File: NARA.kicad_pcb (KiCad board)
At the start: 4 copper layers, 93.9 x 42.4 mm, 144 parts, among them K1 BATT, K10 TOF_LD, K11 TOF_LS, K12 TOF_RF, K13 TOF_RD, K14 TOF_RS, K2 K_FPC_52435-2471, K3 PROG, K5 K_PicoSPOX-3, K6 K_0002, K7 K_PicoSPOX-3, K8 K_0002, K9 TOF_LF, Q1 Q_0004, Q2 Q_0007, Q3 Q_0007, Q4 Q_0007, Q5 Q_0007, Q6 Q_0007, Q7 Q_0007, Q8 Q_0004, Q9 Q_0004, SW1 SW_SKQG, SW2 SW_SKQG, U1 U_LT8610ABIMSE-3.3, U10 QRE1113GR, U11 QRE1113GR, U12 QRE1113GR, U2 U_AP2204K-5.0TRG1, U3 LTC2944, U4 L6234, U5 L6234, U6 LTC2955TS8-1, U7 STM32H743VITx, U8 ICM-20689, U9 QRE1113GR

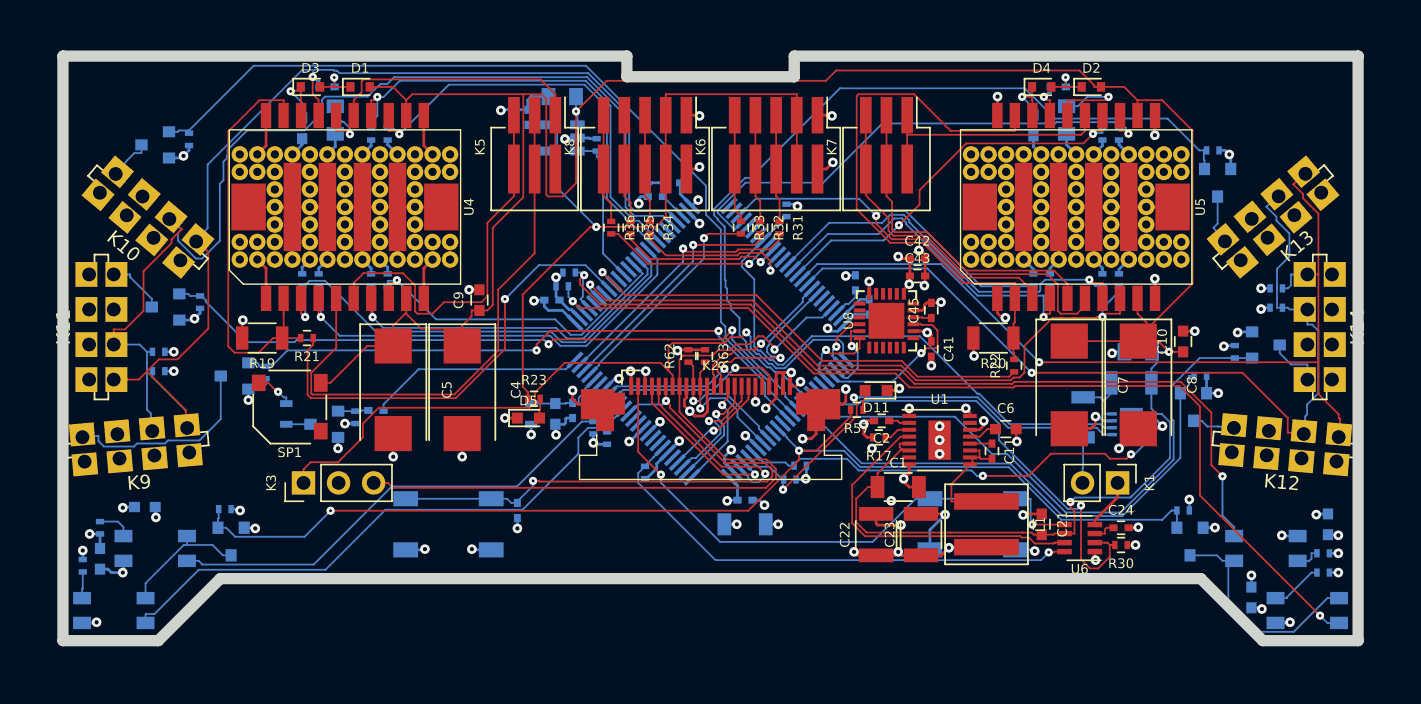
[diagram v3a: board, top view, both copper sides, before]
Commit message: Change EdgeCuts for TOF sensors, adapt power trace lengh
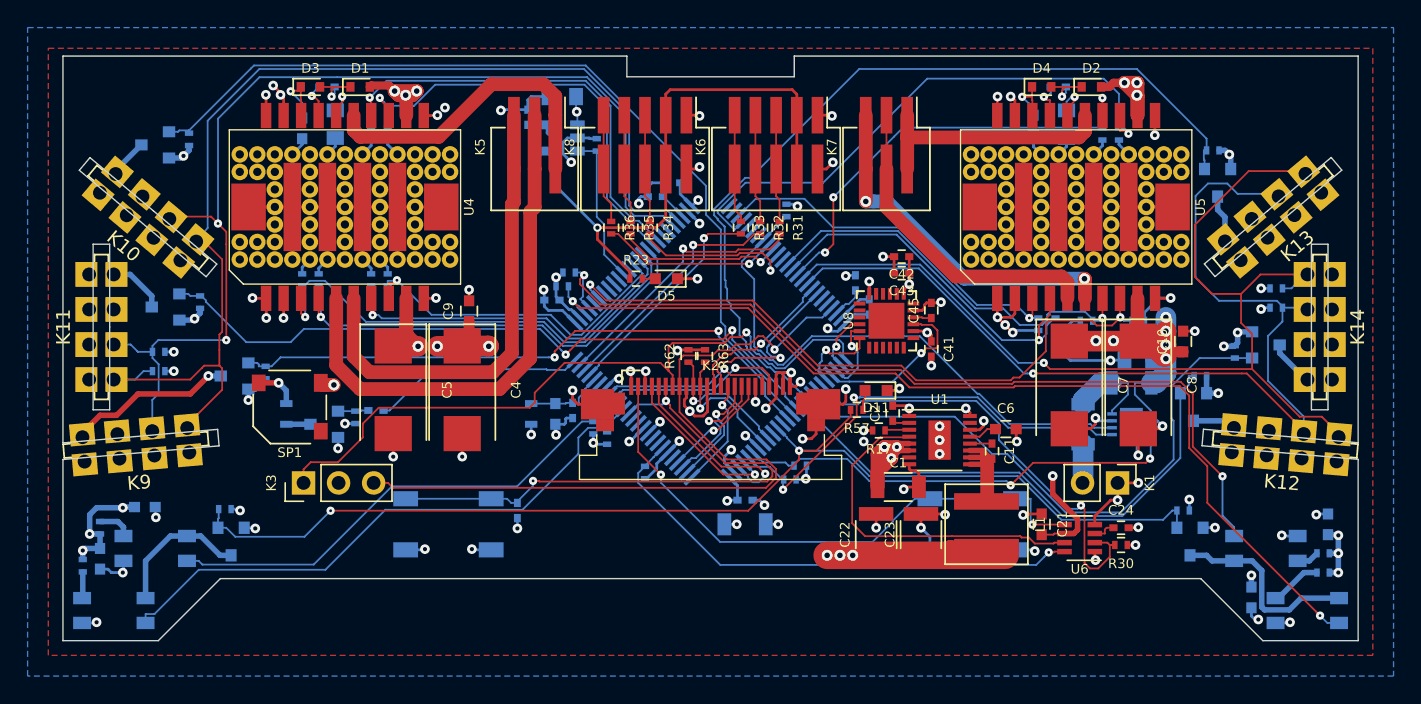
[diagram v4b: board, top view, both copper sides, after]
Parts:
- removed R19, R20: R_0093, DVB_Resistors:R_1206
- removed R21, R22: R_0015, DVB_Resistors:R_0402
- moved D5 14.2 mm to (94.8, 88.2), turned to 180 degrees
- moved R23 11.4 mm to (92.6, 88.2)
- moved R10 3.27 mm to (129.0, 91.2), turned to 180 degrees
- moved R4 3.22 mm to (123.0, 91.5), turned to 90 degrees
- moved R13 3.22 mm to (121.8, 91.5), turned to 90 degrees
- moved R2 3.17 mm to (125.2, 91.2), turned to 0 degrees
- moved C43 1.17 mm to (111.8, 87.8), turned to 180 degrees
- moved C42 1.16 mm to (111.8, 86.6), turned to 180 degrees
- moved C9 1.10 mm to (80.5, 90.5)
- moved C2 0.97 mm to (111.2, 98.0), turned to 90 degrees
- moved C17 0.60 mm to (129.0, 94.1)
- moved F1 0.50 mm to (125.0, 98.8)
- moved R17 0.50 mm to (110.2, 99.2)
- moved C15 0.30 mm to (70.8, 77.0)
- moved C16 0.30 mm to (123.8, 77.0)
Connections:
- U4 pad 19: Net-(R19-Pad1) -> GND
- U4 pad 2: Net-(R19-Pad1) -> GND
- U5 pad 19: Net-(R20-Pad1) -> GND
- U5 pad 2: Net-(R20-Pad1) -> GND
- U7 pad 33: /MOT_L_SENSE -> (no net)
- U7 pad 34: /MOT_R_SENSE -> (no net)
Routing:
- net Net-(R20-Pad1): track 41.2 -> 0.00 mm
- net GND: track 767.1 -> 801.5 mm, vias 76 -> 87
- net /MOT_R_SENSE: track 34.3 -> 0.00 mm, vias 1 -> 0
- net /MOT_L_SENSE: track 33.1 -> 0.00 mm, vias 1 -> 0
- net +BATT: track 189.7 -> 222.7 mm, vias 3 -> 22
- net Net-(R19-Pad1): track 30.4 -> 0.00 mm
- net +3.3V: track 323.2 -> 341.5 mm, vias 42 -> 41
- net /MOT_R_EN2: track 39.2 -> 27.3 mm
- net +5V: track 54.9 -> 44.4 mm
- net /TOF_R_SCL: track 63.8 -> 74.1 mm
- net /TOF_R_SDA: track 65.2 -> 75.4 mm
- net /MOT_L_PHASE_A_BRO: track 27.9 -> 34.0 mm
- net Net-(C16-Pad2): track 7.51 -> 2.93 mm
- net /MOT_R_EN3: track 37.6 -> 41.5 mm
- net /TOF_L_SDA: track 76.7 -> 80.1 mm
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- added copper zone on PWR.Cu, net +3.3V
- added copper zone on PWR.Cu, net +BATT
- added copper zone on B.Cu, net GND
- added copper zone on F.Cu, net GND
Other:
- outline, holes or cut-outs redrawn

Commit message: Save before change vias
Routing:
- net /TOF_L_SDA: track 80.1 -> 78.2 mm
- net Net-(C18-Pad1): track 5.12 -> 4.42 mm
- net Net-(C12-Pad1): track 2.61 -> 2.10 mm
- net GND: track 801.5 -> 801.6 mm, vias 87 -> 88
- net Net-(C15-Pad2): track 3.45 -> 3.39 mm, vias 1 -> 2

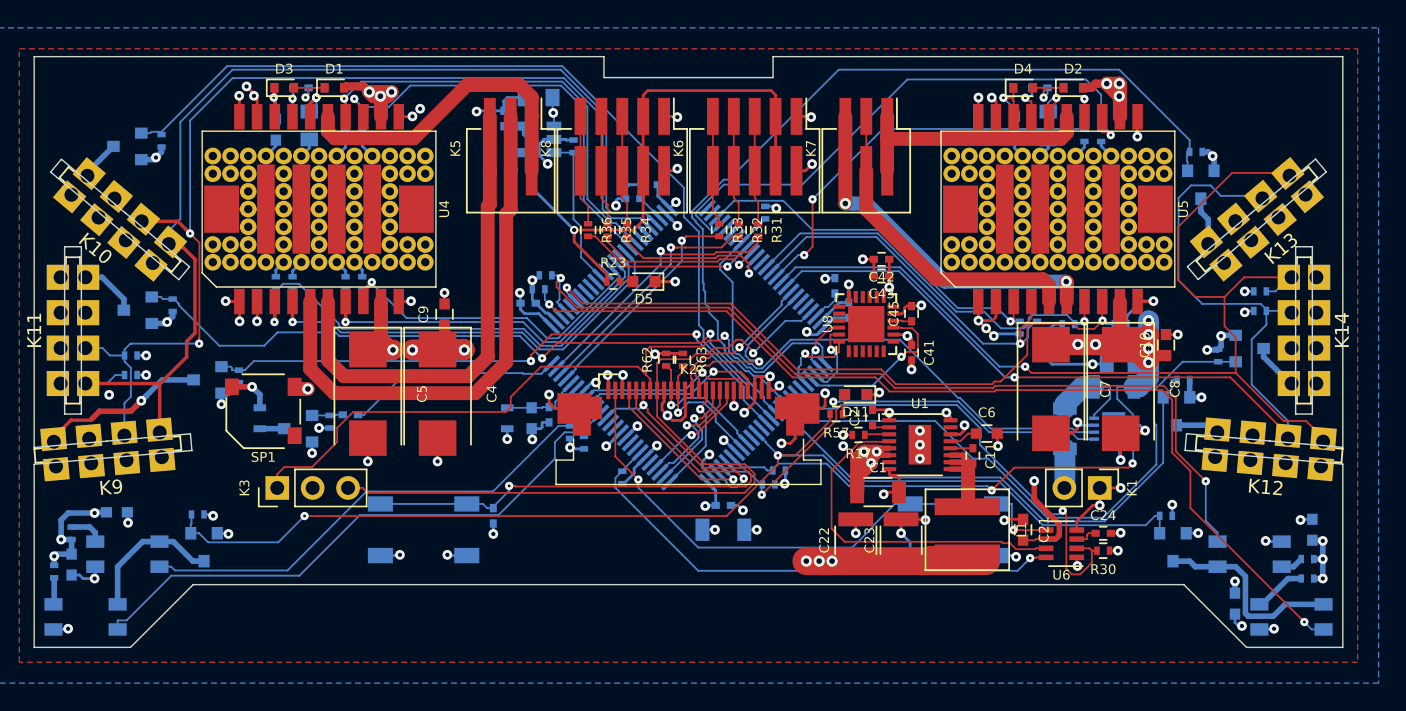
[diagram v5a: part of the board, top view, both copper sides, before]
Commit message: Update via type, route Top, GND, PWR complete
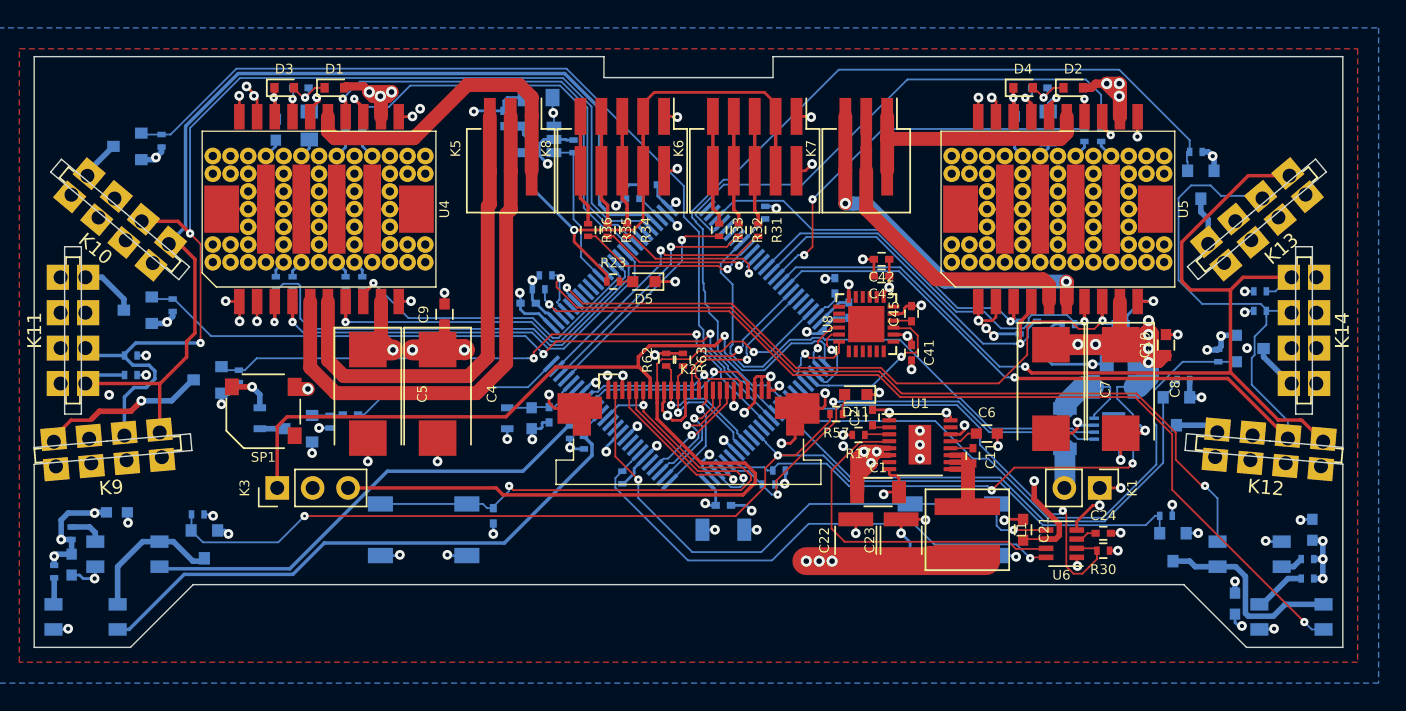
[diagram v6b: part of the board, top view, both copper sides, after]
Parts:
- moved Q8 0.20 mm to (63.3, 107.0)
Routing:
- net /SWCLK: track 51.8 -> 55.0 mm
- net +BATT: track 222.7 -> 225.5 mm
- net /TOF_L_SCL: track 77.8 -> 80.2 mm
- net /BLUETOOTH_RX: track 13.3 -> 11.6 mm
- net /LINE_ADC_R1: track 71.5 -> 70.0 mm
- net /TOF_R_SDA: track 75.4 -> 73.9 mm
- net /LINE_ADC_R2: track 63.6 -> 62.2 mm
- net /WKUP: track 37.0 -> 38.5 mm
- net GND: track 801.6 -> 802.9 mm, vias 88 -> 89
- net /MOT_L_EN2: track 35.2 -> 36.4 mm
- net Net-(C19-Pad1): track 4.48 -> 5.54 mm
- net /TOF_EN_LS: track 51.1 -> 50.2 mm
- net +5V: track 44.4 -> 43.6 mm
- net /BLUETOOTH_TX: track 11.2 -> 12.0 mm
- net +3.3V: track 341.5 -> 342.2 mm
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
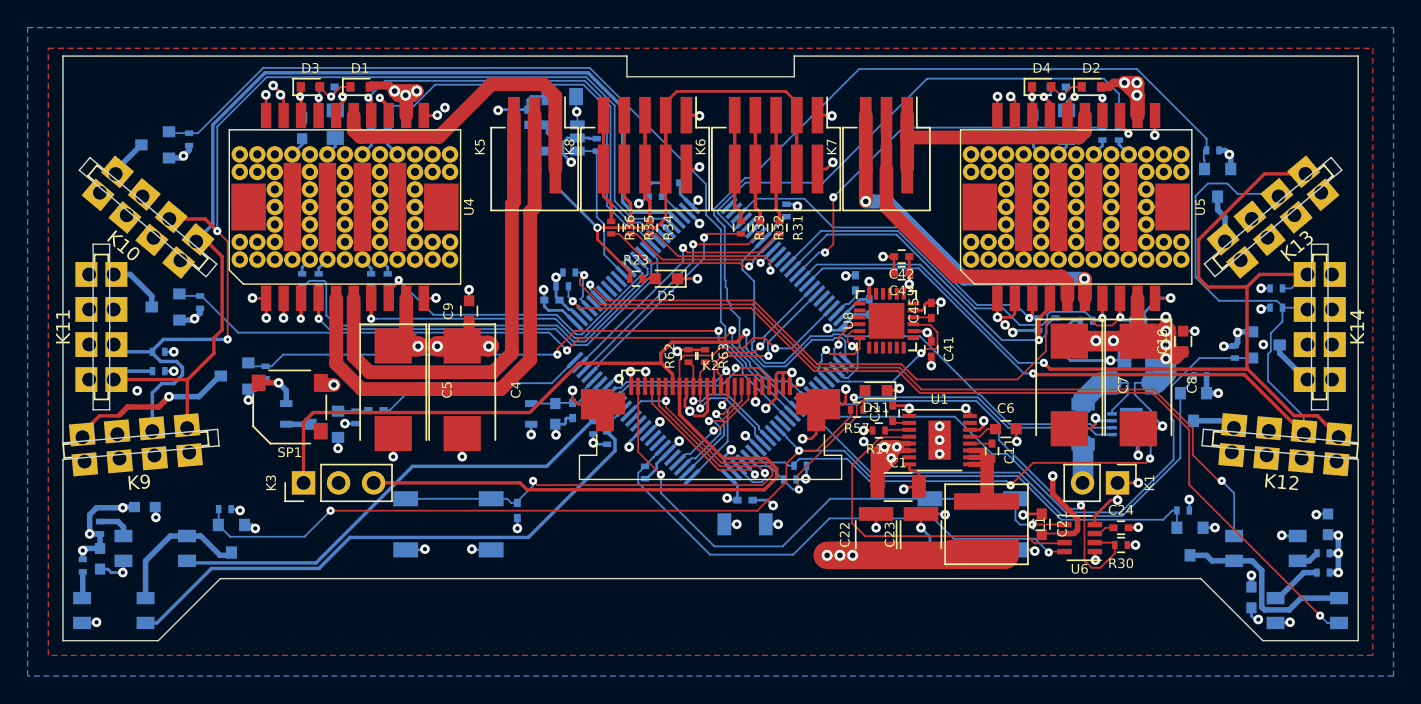
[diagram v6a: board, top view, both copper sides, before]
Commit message: First NARA PCB, v1.0.0-B1
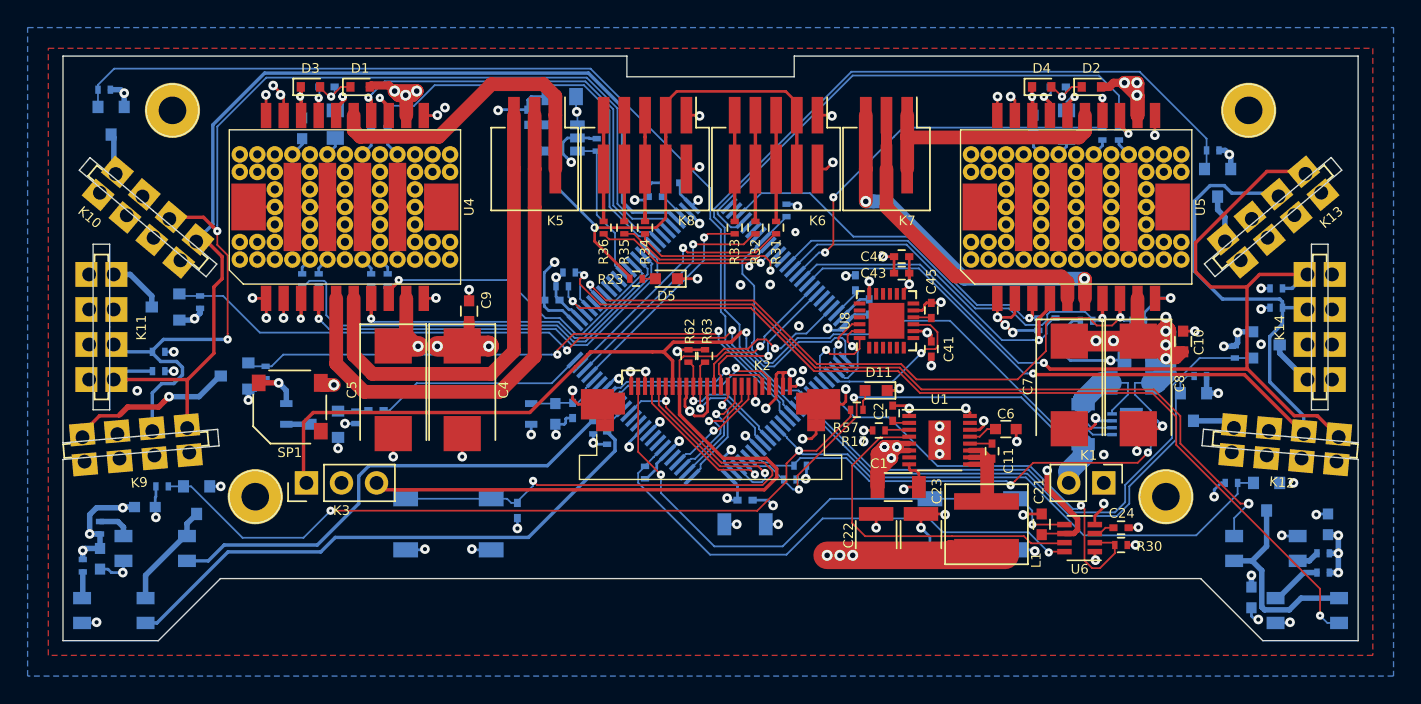
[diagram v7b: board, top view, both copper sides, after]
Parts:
- added REF**: VAL**, DVB_Mechanicals:Drill_2.6mm, F.Cu at (59.0, 76.0)
- added REF**: VAL**, DVB_Mechanicals:Drill_2.6mm, F.Cu at (65.0, 104.0)
- added REF**: VAL**, DVB_Mechanicals:Drill_2.6mm, F.Cu at (131.0, 104.0)
- added REF**: VAL**, DVB_Mechanicals:Drill_2.6mm, F.Cu at (137.0, 76.0)
- moved R40 7.13 mm to (54.0, 74.5), turned to 180 degrees
- moved Q9 6.43 mm to (138.3, 104.0)
- moved R45 4.84 mm to (58.2, 103.2), turned to 0 degrees
- moved R46 4.03 mm to (135.8, 103.0), turned to 0 degrees
- moved Q8 3.77 mm to (60.8, 104.2)
- moved Q3 3.65 mm to (54.5, 76.8), turned to 0 degrees
- moved K1 1.00 mm to (126.5, 103.0)
- moved R36 0.55 mm to (90.2, 84.5)
- moved R33 0.45 mm to (99.8, 84.5)
- moved R35 0.45 mm to (91.8, 84.5)
- moved R32 0.35 mm to (101.2, 84.5)
- moved R34 0.35 mm to (93.2, 84.5)
- moved R31 0.25 mm to (102.8, 84.5)
- moved K3 0.21 mm to (68.7, 103.0)
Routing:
- net GND: track 802.9 -> 834.0 mm, vias 89 -> 93
- net /LINE_EN: track 85.5 -> 95.7 mm
- net +3.3V: track 342.2 -> 350.0 mm
- net /TOF_EN_LD: track 63.6 -> 68.9 mm
- net Net-(Q8-Pad3): track 10.2 -> 7.72 mm
- net /SWCLK: track 55.0 -> 53.2 mm
- net /LINE_ADC_R2: track 62.2 -> 63.3 mm
- net /LINE_ADC_L2: track 36.1 -> 37.2 mm
- net /FUEL_GAUGE_~ALCC: track 41.5 -> 42.3 mm
- net /MOT_R_IN2: track 27.6 -> 27.0 mm
- net /MOT_R_IN1: track 29.1 -> 28.5 mm
- net /MOT_R_HALL1: track 13.1 -> 13.7 mm
